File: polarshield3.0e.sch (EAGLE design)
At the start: 45 parts, among them CN1 DIP-BLACK-FEMALE-HEADER-VERT(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, CN2 DIP-BLACK-FEMALE-HEADER-VERT(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, Q4 BSS138, Q5 BSS138, Q6 BSS138, Q7 BSS138

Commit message: v3.0e rebuilt
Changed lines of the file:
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@@
 <wire x1="-93.98" y1="127" x2="-104.14" y2="127" width="0.1524" layer="91"/>
 <junction x="-93.98" y="127"/>
+<junction x="-104.14" y="127"/>
 </segment>
 <segment>
@@
 <wire x1="20.32" y1="88.9" x2="15.24" y2="88.9" width="0.1524" layer="91"/>
 <pinref part="+3V4" gate="G$1" pin="+3V3"/>
+<junction x="15.24" y="99.06"/>
+<junction x="15.24" y="88.9"/>
 </segment>
 <segment>
@@
 <wire x1="20.32" y1="-2.54" x2="15.24" y2="-2.54" width="0.1524" layer="91"/>
 <pinref part="+3V9" gate="G$1" pin="+3V3"/>
-</segment>
-<segment>
+<junction x="15.24" y="-2.54"/>
+<junction x="15.24" y="7.62"/>
+</segment>
+<segment>

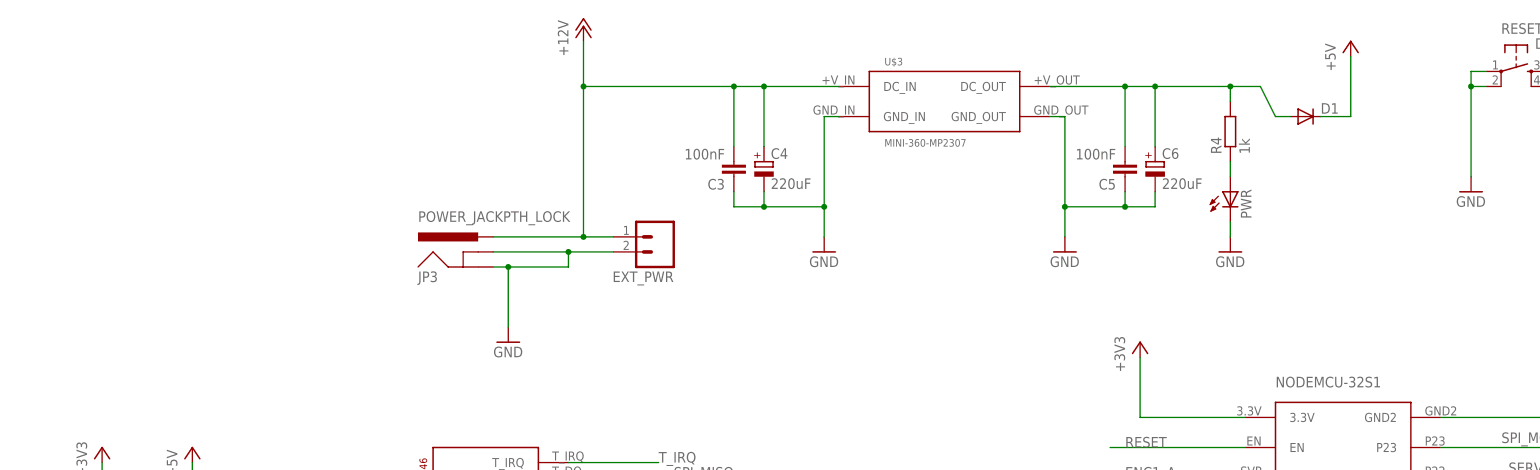
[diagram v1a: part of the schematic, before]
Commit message: Added part number GF1A-E3/67A to D1, #1
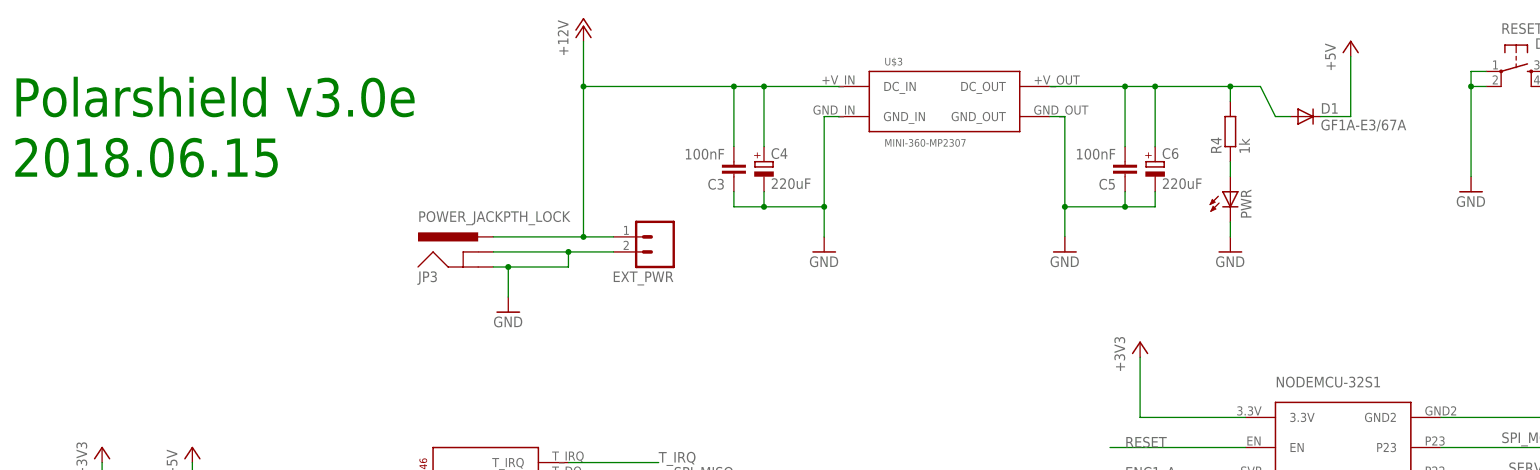
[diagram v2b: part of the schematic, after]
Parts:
- D1: value (none) -> GF1A-E3/67A
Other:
- note added: "2018.06.15"
- note added: "Polarshield v3.0e"
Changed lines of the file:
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@@
 <part name="RX" library="polargraph3" deviceset="LED" device="CHIPLED_0805"/>
 <part name="+3V7" library="supply1" deviceset="+3V3" device=""/>
-<part name="D1" library="diode" deviceset="DIODE-" device="DO214BA"/>
+<part name="D1" library="diode" deviceset="DIODE-" device="DO214BA" value="GF1A-E3/67A "/>
 <part name="P+4" library="supply1" deviceset="+5V" device=""/>
 <part name="+3V8" library="supply1" deviceset="+3V3" device=""/>
@@
 <wire x1="7.62" y1="-55.88" x2="7.62" y2="30.48" width="0.1524" layer="90"/>
 <text x="58.42" y="20.32" size="6.4516" layer="90">Motor 2</text>
+<text x="-281.94" y="142.24" size="6.4516" layer="91">Polarshield v3.0e</text>
+<text x="-281.94" y="132.08" size="6.4516" layer="91">2018.06.15</text>
+<wire x1="-292.1" y1="165.1" x2="147.32" y2="165.1" width="1.016" layer="90"/>
+<wire x1="147.32" y1="165.1" x2="147.32" y2="-63.5" width="1.016" layer="90"/>
+<wire x1="147.32" y1="-63.5" x2="-45.72" y2="-63.5" width="1.016" layer="90"/>
+<wire x1="-45.72" y1="-63.5" x2="-226.06" y2="-63.5" width="1.016" layer="90"/>
+<wire x1="-226.06" y1="-63.5" x2="-292.1" y2="-63.5" width="1.016" layer="90"/>
+<wire x1="-292.1" y1="-63.5" x2="-292.1" y2="99.06" width="1.016" layer="90"/>
+<wire x1="-292.1" y1="99.06" x2="-292.1" y2="165.1" width="1.016" layer="90"/>
+<wire x1="-292.1" y1="99.06" x2="-226.06" y2="99.06" width="1.016" layer="90"/>
+<wire x1="-226.06" y1="99.06" x2="-226.06" y2="-15.24" width="1.016" layer="90"/>
+<wire x1="-226.06" y1="-15.24" x2="-226.06" y2="-63.5" width="1.016" layer="90"/>
+<wire x1="-226.06" y1="-15.24" x2="-144.78" y2="-15.24" width="1.016" layer="90"/>
+<wire x1="-144.78" y1="-15.24" x2="-144.78" y2="99.06" width="1.016" layer="90"/>
+<wire x1="-144.78" y1="99.06" x2="-226.06" y2="99.06" width="1.016" layer="90"/>
+<wire x1="-144.78" y1="-15.24" x2="-45.72" y2="-15.24" width="1.016" layer="90"/>
+<wire x1="-45.72" y1="-15.24" x2="-45.72" y2="-63.5" width="1.016" layer="90"/>
 </plain>
 <instances>
@@
 <instance part="GND10" gate="1" x="-144.78" y="119.38"/>
 <instance part="JP3" gate="G$1" x="-203.2" y="114.3"/>
-<instance part="GND11" gate="1" x="-198.12" y="104.14"/>
+<instance part="GND11" gate="1" x="-198.12" y="109.22"/>
 <instance part="EXT_PWR" gate="G$1" x="-172.72" y="121.92" rot="R180"/>
 <instance part="P+3" gate="1" x="-185.42" y="157.48"/>
@@
 <pinref part="GND11" gate="1" pin="GND"/>
 <wire x1="-198.12" y1="116.84" x2="-200.66" y2="116.84" width="0.1524" layer="91"/>
-<wire x1="-198.12" y1="106.68" x2="-198.12" y2="116.84" width="0.1524" layer="91"/>
+<wire x1="-198.12" y1="111.76" x2="-198.12" y2="116.84" width="0.1524" layer="91"/>
 <pinref part="EXT_PWR" gate="G$1" pin="2"/>
 <wire x1="-187.96" y1="119.38" x2="-180.34" y2="119.38" width="0.1524" layer="91"/>
